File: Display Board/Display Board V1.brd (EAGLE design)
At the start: 52.5 x 30 mm, 3 parts, among them K1 FFC/FPC/34PIN/1MMPITCH/TOPLOCK

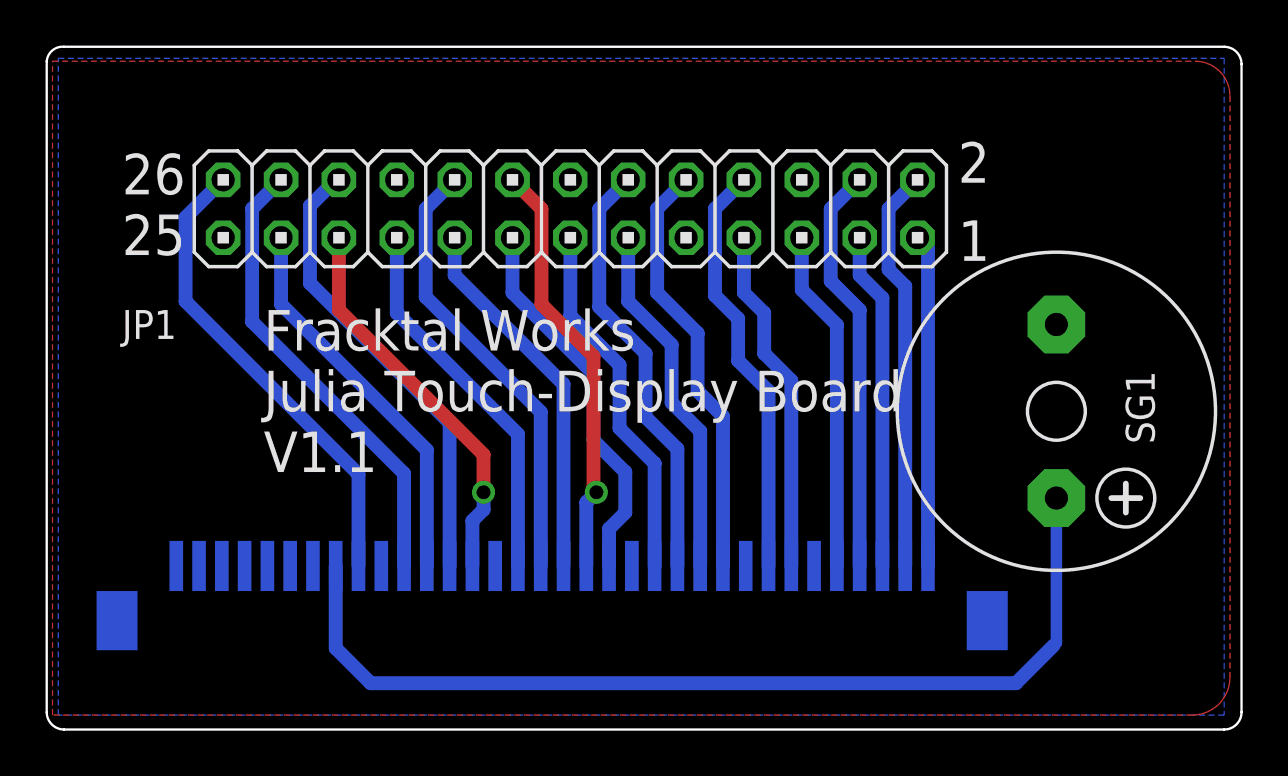
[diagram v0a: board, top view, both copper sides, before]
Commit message: added display board gerbers
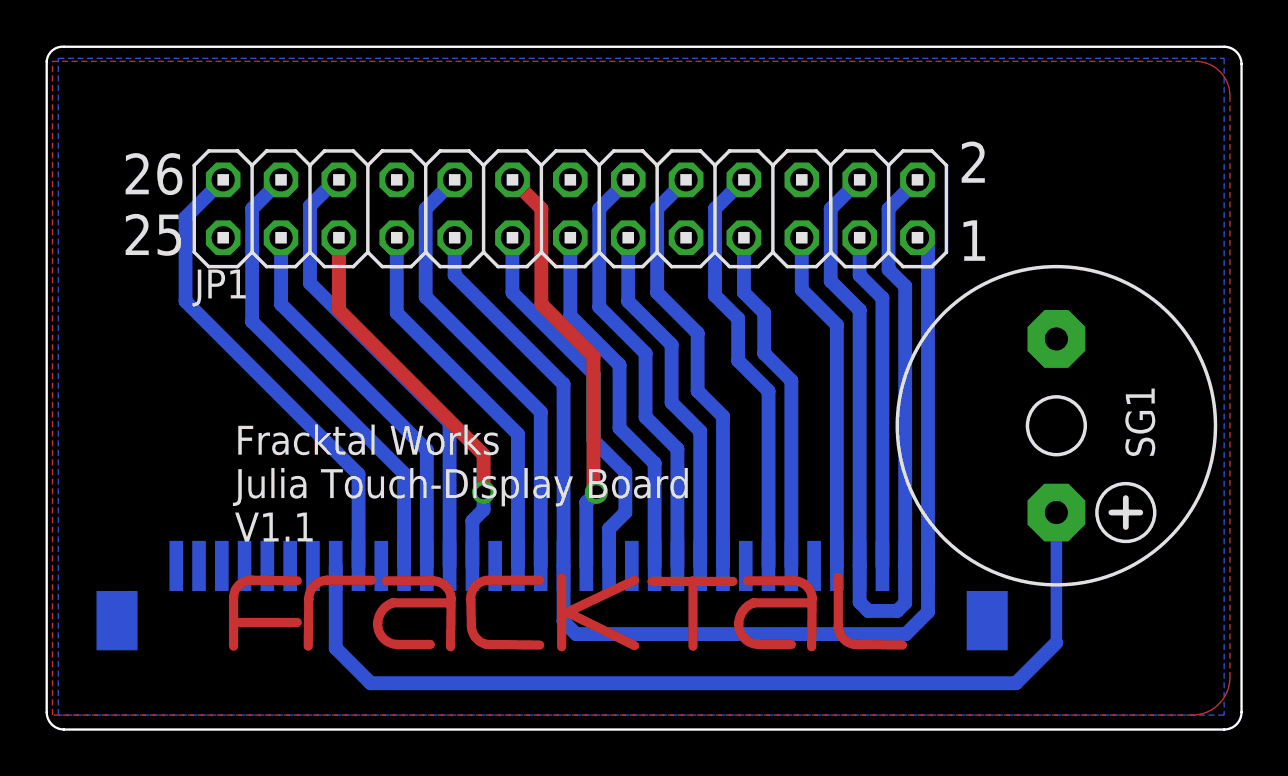
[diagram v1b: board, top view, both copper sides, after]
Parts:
- added U$1: FRACKTALLOGO, FracktalWorks_Eagle_Library:FRACKTALLOGO
- moved SG1 0.63 mm to (44.2, 13.3)
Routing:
- net 3V3: track 31.0 -> 52.1 mm
- net 5V: track 35.8 -> 41.3 mm
- net BUZZER: track 43.0 -> 42.3 mm
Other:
- board text added: "Corner Of Display Here"
- board text removed: "Display Corner Here"
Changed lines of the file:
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@@
 <board>
 <plain>
-<text x="9.398" y="11.303" size="1.778" layer="21" rot="SR0">Fracktal Works
+<text x="8.128" y="8.255" size="1.27" layer="21" rot="SR0">Fracktal Works
 Julia Touch-Display Board
 V1.1</text>
@@
 <wire x1="41.91" y1="28.321" x2="41.021" y2="27.432" width="0.508" layer="22"/>
 <wire x1="41.021" y1="27.432" x2="41.91" y2="26.543" width="0.508" layer="22"/>
-<text x="47.625" y="25.908" size="1.778" layer="22" rot="MR270">Display Corner Here</text>
+<text x="51.054" y="27.559" size="1.016" layer="22" rot="SMR270">Corner Of Display Here</text>
 <text x="3.175" y="20.828" size="1.778" layer="21">25</text>
 <text x="3.175" y="23.495" size="1.778" layer="21">26</text>
@@
 </class>
 </classes>
-<designrules name="default *">
+<designrules name="LionCircuits">
 <description language="de">&lt;b&gt;EAGLE Design Rules&lt;/b&gt;
 &lt;p&gt;
@@
 <param name="mdSmdVia" value="8mil"/>
 <param name="mdSmdSmd" value="8mil"/>
-<param name="mdViaViaSameLayer" value="8mil"/>
+<param name="mdViaViaSameLayer" value="6mil"/>
 <param name="mnLayersViaInSmd" value="2"/>
-<param name="mdCopperDimension" value="40mil"/>
+<param name="mdCopperDimension" value="60mil"/>
 <param name="mdDrill" value="10mil"/>
 <param name="mdSmdStop" value="0mil"/>
-<param name="msWidth" value="18mil"/>
+<param name="msWidth" value="8mil"/>
 <param name="msDrill" value="0.35mm"/>
 <param name="msMicroVia" value="9.99mm"/>
@@
 <attribute name="VALUE" x="37.9416" y="3.7766" size="1.27" layer="28" rot="MR0"/>
 </element>
-<element name="SG1" library="buzzer" package="F/CM12P" value="F/CM12P" x="44.196" y="13.97" smashed="yes" rot="R270">
-<attribute name="MF" value="" x="44.196" y="13.97" size="1.778" layer="27" rot="R270" display="off"/>
-<attribute name="MPN" value="" x="44.196" y="13.97" size="1.778" layer="27" rot="R270" display="off"/>
-<attribute name="NAME" x="47.244" y="15.748" size="1.27" layer="25" ratio="10" rot="R270"/>
-<attribute name="OC_FARNELL" value="unknown" x="44.196" y="13.97" size="1.778" layer="27" rot="R270" display="off"/>
-<attribute name="OC_NEWARK" value="unknown" x="44.196" y="13.97" size="1.778" layer="27" rot="R270" display="off"/>
-<attribute name="VALUE" x="40.386" y="18.415" size="1.27" layer="27" ratio="10" rot="R270"/>
+<element name="SG1" library="buzzer" package="F/CM12P" value="F/CM12P" x="44.196" y="13.335" smashed="yes" rot="R270">
+<attribute name="MF" value="" x="44.196" y="13.335" size="1.778" layer="27" rot="R270" display="off"/>
+<attribute name="MPN" value="" x="44.196" y="13.335" size="1.778" layer="27" rot="R270" display="off"/>
+<attribute name="NAME" x="47.244" y="15.113" size="1.27" layer="25" ratio="10" rot="R270"/>
+<attribute name="OC_FARNELL" value="unknown" x="44.196" y="13.335" size="1.778" layer="27" rot="R270" display="off"/>
+<attribute name="OC_NEWARK" value="unknown" x="44.196" y="13.335" size="1.778" layer="27" rot="R270" display="off"/>
+<attribute name="VALUE" x="40.386" y="17.78" size="1.27" layer="27" ratio="10" rot="R270"/>
 </element>
 <element name="JP1" library="pinhead" library_urn="urn:adsk.eagle:library:325" package="2X13" package3d_urn="urn:adsk.eagle:package:22418/2" value="" x="22.86" y="22.86" smashed="yes">
-<attribute name="NAME" x="3.175" y="17.145" size="1.27" layer="25" ratio="10"/>
+<attribute name="NAME" x="6.35" y="18.923" size="1.27" layer="25" ratio="10"/>
 <attribute name="VALUE" x="6.35" y="18.415" size="1.27" layer="27"/>
 </element>
+<element name="U$1" library="FracktalWorks_Eagle_Library" package="FRACKTALLOGO" value="FRACKTALLOGO" x="20.066" y="3.556" smashed="yes"/>
 </elements>
 <signals>
@@
 <wire x1="17.78" y1="19.939" x2="17.78" y2="21.59" width="0.6096" layer="16"/>
 <wire x1="22.56" y1="15.159" x2="17.78" y2="19.939" width="0.6096" layer="16"/>
-<wire x1="22.56" y1="7.18" x2="38.56" y2="7.18" width="0" layer="19" extent="16-16"/>
+<wire x1="22.56" y1="7.18" x2="22.56" y2="4.745" width="0.6096" layer="16"/>
+<wire x1="22.56" y1="4.745" x2="23.114" y2="4.191" width="0.6096" layer="16"/>
+<wire x1="23.114" y1="4.191" x2="37.592" y2="4.191" width="0.6096" layer="16"/>
+<wire x1="38.56" y1="5.159" x2="38.56" y2="7.18" width="0.6096" layer="16"/>
+<wire x1="37.592" y1="4.191" x2="38.56" y2="5.159" width="0.6096" layer="16"/>
 </signal>
 <signal name="5V">
@@
 <wire x1="34.29" y1="19.685" x2="34.29" y2="22.86" width="0.6096" layer="16"/>
 <wire x1="34.29" y1="22.86" x2="35.56" y2="24.13" width="0.6096" layer="16"/>
-<wire x1="35.56" y1="24.13" x2="36.83" y2="22.86" width="0" layer="19" extent="16-16"/>
+<wire x1="35.56" y1="7.18" x2="35.56" y2="5.588" width="0.6096" layer="16"/>
+<wire x1="35.941" y1="5.207" x2="35.56" y2="5.588" width="0.6096" layer="16"/>
+<wire x1="37.56" y1="7.18" x2="37.56" y2="5.556" width="0.6096" layer="16"/>
+<wire x1="37.211" y1="5.207" x2="35.941" y2="5.207" width="0.6096" layer="16"/>
+<wire x1="37.56" y1="5.556" x2="37.211" y2="5.207" width="0.6096" layer="16"/>
 </signal>
 <signal name="GND">
@@
 <wire x1="12.56" y1="3.569" x2="14.097" y2="2.032" width="0.6096" layer="16"/>
 <wire x1="14.097" y1="2.032" x2="42.418" y2="2.032" width="0.6096" layer="16"/>
-<wire x1="44.069" y1="3.683" x2="42.418" y2="2.032" width="0.6096" layer="16"/>
-<wire x1="44.196" y1="10.16" x2="44.196" y2="3.81" width="0.508" layer="16"/>
-<wire x1="44.196" y1="3.81" x2="44.069" y2="3.683" width="0.508" layer="16"/>
+<wire x1="44.196" y1="3.81" x2="42.418" y2="2.032" width="0.6096" layer="16"/>
+<wire x1="44.196" y1="9.525" x2="44.196" y2="3.81" width="0.508" layer="16"/>
 </signal>
 </signals>
@@
 <mfgpreviewcolor name="substratecolor" color="0xFF786E46"/>
 </mfgpreviewcolors>
-<errors>
-</errors>
 </board>
 </drawing>
